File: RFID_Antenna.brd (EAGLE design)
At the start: 25.4 x 43.2 mm, 25 parts, among them J1 U.FL

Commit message: Caopy Murata Design w/ Transparency for x02
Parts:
- C1, C2, C3, C4, C5, C6, L1, R1: device special_parts:0402 -> special_parts:0402_MURATA
- L2, L3, L4, L5: device special_parts:0603 -> special_parts:0603_MURATA
- moved L5 4.23 mm to (11.9, 18.1)
- moved C6 4.19 mm to (14.4, 18.1)
- moved C5 4.14 mm to (11.6, 19.4)
- moved L4 3.97 mm to (14.1, 19.4)
- moved L1 3.65 mm to (13.0, 20.5)
- moved J1 3.50 mm to (12.5, 14.5)
- moved C3 3.34 mm to (12.5, 22.0)
- moved C4 3.31 mm to (13.3, 22.1)
- moved L2 2.91 mm to (11.4, 21.1)
- moved L3 2.81 mm to (14.6, 21.2)
- moved C1 2.61 mm to (12.1, 23.2)
- moved C2 2.52 mm to (13.7, 23.2)
- moved R1 0.46 mm to (13.0, 24.1)
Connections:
- net A1: now also C1.P$1, L2.P$2, R1.P$1; no longer C1.1, L2.2, R1.1
- net A2: now also C2.P$2, L3.P$2, R1.P$2; no longer C2.2, L3.2, R1.2
- net C1C3: now also C1.P$2, C3.P$1; no longer C1.2, C3.1
- net C2C4: now also C2.P$1, C4.P$1; no longer C2.1, C4.1
- net C3C4: now also C3.P$2, C4.P$2; no longer C3.2, C4.2
- net GND: now also C5.P$1, L4.P$2; no longer C5.1, L4.2
- net L5C6: now also C6.P$2, L5.P$1; no longer C6.2, L5.1
- net N$6: now also C6.P$1, L1.P$2, L3.P$1, L4.P$1; no longer C6.1, L1.2, L3.1, L4.1
- net N$7: now also C5.P$2, L1.P$1, L2.P$1, L5.P$2; no longer C5.2, L1.1, L2.1, L5.2
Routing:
- net A1: track 5.55 -> 1.44 mm
- net A2: track 5.61 -> 2.81 mm
- net N$6: track 5.93 -> 3.62 mm
- net N$7: track 5.50 -> 3.61 mm
- net GND: track 1.84 -> 2.58 mm, vias 19 -> 25
- net C2C4: track 1.37 -> 0.75 mm
- net C1C3: track 1.37 -> 0.78 mm
- net C3C4: track 1.40 -> 0.83 mm

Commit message: Add production for x02
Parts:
- moved FRAME1 113.1 mm to (-15.2, -66.0)
- moved U$2 66.1 mm to (-34.3, -5.08)
- moved U$11 12.7 mm to (12.7, 25.4)
- moved C2 5.08 mm to (13.7, 18.1)
- moved C3 5.08 mm to (12.5, 17.0)
- moved L3 5.08 mm to (14.6, 16.1)
- moved U$1 5.08 mm to (12.7, 26.7)
- moved U$3 5.08 mm to (12.7, 28.6)
- moved U$4 5.08 mm to (12.7, 28.6)
- moved U$5 5.08 mm to (6.83, 25.9)
- moved U$6 5.08 mm to (18.5, 25.9)
- moved J1 5.08 mm to (12.5, 9.42)
- moved L1 5.08 mm to (13.0, 15.4)
- moved L4 5.08 mm to (14.1, 14.3)
- moved L5 5.08 mm to (11.9, 13.0)
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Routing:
- net GND: track 2.58 -> 2.80 mm, vias 25 -> 24
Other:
- board size 25.4 x 43.2 mm -> 25.4 x 38.1 mm
- board text added: "Owen Lyke"

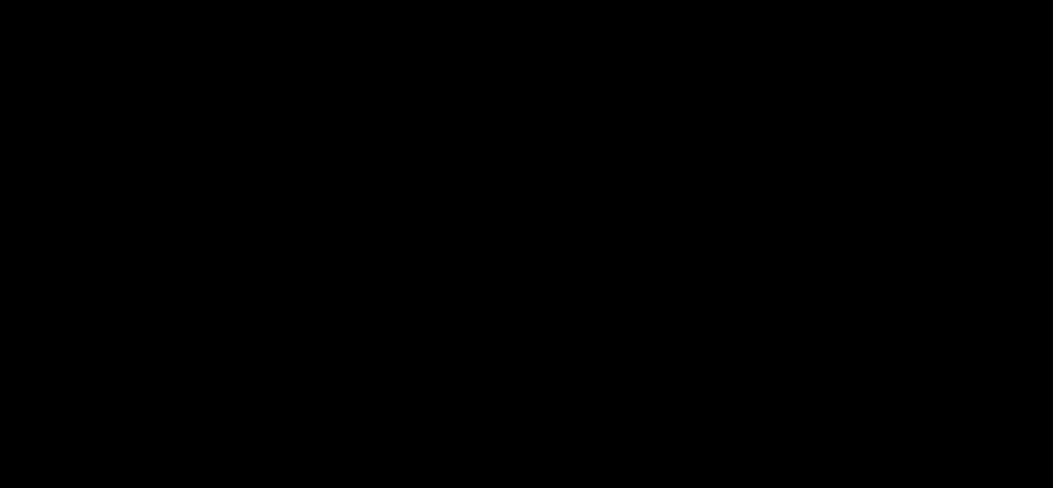
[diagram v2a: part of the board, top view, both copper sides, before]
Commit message: Prettified schematic (and fixed component values)
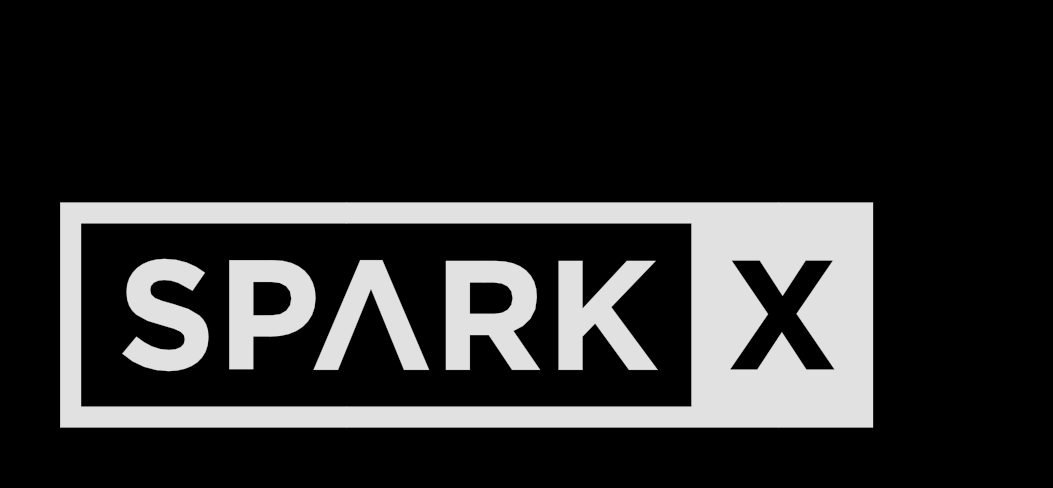
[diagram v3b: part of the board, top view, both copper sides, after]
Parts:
- added U$12: SPARKX-LOGO6, SparkX:SPARKX-XLARGE
- C1, C2: value 9.3 pF -> 5.0 pF
- C3, C4: value 9.0 pF -> 5.0 pF
- C5, C6: value 5.66 pF -> 2.4 pF
- L1: value 0.26 uH -> 19 nH
- L2, L3: value 0.26 uH -> 24 nH
- L4, L5: value 0.24 uH -> 11 nH
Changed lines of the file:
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@@
 <grid distance="0.05" unitdist="inch" unit="inch" style="lines" multiple="1" display="yes" altdistance="0.005" altunitdist="inch" altunit="inch"/>
 <layers>
-<layer number="1" name="Top" color="4" fill="1" visible="no" active="yes"/>
-<layer number="16" name="Bottom" color="1" fill="1" visible="no" active="yes"/>
-<layer number="17" name="Pads" color="2" fill="1" visible="no" active="yes"/>
-<layer number="18" name="Vias" color="2" fill="1" visible="no" active="yes"/>
-<layer number="19" name="Unrouted" color="6" fill="1" visible="no" active="yes"/>
+<layer number="1" name="Top" color="4" fill="1" visible="yes" active="yes"/>
+<layer number="16" name="Bottom" color="1" fill="1" visible="yes" active="yes"/>
+<layer number="17" name="Pads" color="2" fill="1" visible="yes" active="yes"/>
+<layer number="18" name="Vias" color="2" fill="1" visible="yes" active="yes"/>
+<layer number="19" name="Unrouted" color="6" fill="1" visible="yes" active="yes"/>
 <layer number="20" name="Dimension" color="15" fill="1" visible="yes" active="yes"/>
-<layer number="21" name="tPlace" color="16" fill="1" visible="no" active="yes"/>
-<layer number="22" name="bPlace" color="14" fill="1" visible="no" active="yes"/>
-<layer number="23" name="tOrigins" color="15" fill="1" visible="no" active="yes"/>
-<layer number="24" name="bOrigins" color="15" fill="1" visible="no" active="yes"/>
+<layer number="21" name="tPlace" color="16" fill="1" visible="yes" active="yes"/>
+<layer number="22" name="bPlace" color="14" fill="1" visible="yes" active="yes"/>
+<layer number="23" name="tOrigins" color="15" fill="1" visible="yes" active="yes"/>
+<layer number="24" name="bOrigins" color="15" fill="1" visible="yes" active="yes"/>
 <layer number="25" name="tNames" color="7" fill="1" visible="no" active="yes"/>
 <layer number="26" name="bNames" color="7" fill="1" visible="no" active="yes"/>
 <layer number="27" name="tValues" color="7" fill="1" visible="no" active="yes"/>
 <layer number="28" name="bValues" color="7" fill="1" visible="no" active="yes"/>
-<layer number="29" name="tStop" color="7" fill="3" visible="yes" active="yes"/>
+<layer number="29" name="tStop" color="7" fill="3" visible="no" active="yes"/>
 <layer number="30" name="bStop" color="7" fill="6" visible="no" active="yes"/>
 <layer number="31" name="tCream" color="7" fill="4" visible="no" active="yes"/>
@@
 <layer number="43" name="vRestrict" color="2" fill="10" visible="no" active="yes"/>
 <layer number="44" name="Drills" color="7" fill="1" visible="no" active="yes"/>
-<layer number="45" name="Holes" color="7" fill="1" visible="no" active="yes"/>
+<layer number="45" name="Holes" color="7" fill="1" visible="yes" active="yes"/>
 <layer number="46" name="Milling" color="3" fill="1" visible="no" active="yes"/>
-<layer number="47" name="Measures" color="7" fill="1" visible="no" active="yes"/>
+<layer number="47" name="Measures" color="7" fill="1" visible="yes" active="yes"/>
 <layer number="48" name="Document" color="7" fill="1" visible="no" active="yes"/>
 <layer number="49" name="Reference" color="7" fill="1" visible="no" active="yes"/>
 <layer number="50" name="dxf" color="7" fill="1" visible="no" active="yes"/>
-<layer number="51" name="tDocu" color="6" fill="1" visible="no" active="yes"/>
+<layer number="51" name="tDocu" color="6" fill="1" visible="yes" active="yes"/>
 <layer number="52" name="bDocu" color="7" fill="1" visible="no" active="yes"/>
 <layer number="91" name="Nets" color="2" fill="1" visible="no" active="no"/>
@@
 </autorouter>
 <elements>
-<element name="C1" library="special_parts" package="0402_MURATA" value="9.3 pF" x="12.1462" y="18.1292"/>
-<element name="C2" library="special_parts" package="0402_MURATA" value="9.3 pF" x="13.7462" y="18.1242"/>
-<element name="C3" library="special_parts" package="0402_MURATA" value="9.0 pF" x="12.5192" y="16.9652" rot="R270"/>
-<element name="C4" library="special_parts" package="0402_MURATA" value="9.0 pF" x="13.3412" y="16.9752" rot="R270"/>
-<element name="C5" library="special_parts" package="0402_MURATA" value="5.66 pF" x="11.6212" y="14.3352" rot="R180"/>
-<element name="C6" library="special_parts" package="0402_MURATA" value="5.66 pF" x="14.3952" y="13.0242" rot="R180"/>
+<element name="C1" library="special_parts" package="0402_MURATA" value="5.0 pF" x="12.1462" y="18.1292"/>
+<element name="C2" library="special_parts" package="0402_MURATA" value="5.0 pF" x="13.7462" y="18.1242"/>
+<element name="C3" library="special_parts" package="0402_MURATA" value="5.0 pF" x="12.5192" y="16.9652" rot="R270"/>
+<element name="C4" library="special_parts" package="0402_MURATA" value="5.0 pF" x="13.3412" y="16.9752" rot="R270"/>
+<element name="C5" library="special_parts" package="0402_MURATA" value="2.4 pF" x="11.6212" y="14.3352" rot="R180"/>
+<element name="C6" library="special_parts" package="0402_MURATA" value="2.4 pF" x="14.3952" y="13.0242" rot="R180"/>
 <element name="FRAME1" library="SparkFun-Aesthetics" package="CREATIVE_COMMONS" value="FRAME-LETTER" x="-15.24" y="-66.04">
 <attribute name="DESIGNER" value="Owen Lyke" x="-15.24" y="-66.04" size="1.778" layer="27" display="off"/>
@@
 <attribute name="SF_ID" value="WRL-09144" x="12.5492" y="9.4182" size="1.778" layer="27" rot="R90" display="off"/>
 </element>
-<element name="L1" library="special_parts" package="0402_MURATA" value="0.26 uH" x="13.0092" y="15.3952"/>
-<element name="L2" library="special_parts" package="0603_MURATA" value="0.26 uH" x="11.45" y="16.07" rot="R90"/>
-<element name="L3" library="special_parts" package="0603_MURATA" value="0.26 uH" x="14.575" y="16.08" rot="R90"/>
-<element name="L4" library="special_parts" package="0603_MURATA" value="0.24 uH" x="14.0862" y="14.3282" rot="R180"/>
-<element name="L5" library="special_parts" package="0603_MURATA" value="0.24 uH" x="11.8592" y="13.0392" rot="R180"/>
+<element name="L1" library="special_parts" package="0402_MURATA" value="19 nH" x="13.0092" y="15.3952"/>
+<element name="L2" library="special_parts" package="0603_MURATA" value="24 nH" x="11.45" y="16.07" rot="R90"/>
+<element name="L3" library="special_parts" package="0603_MURATA" value="24 nH" x="14.575" y="16.08" rot="R90"/>
+<element name="L4" library="special_parts" package="0603_MURATA" value="11 nH" x="14.0862" y="14.3282" rot="R180"/>
+<element name="L5" library="special_parts" package="0603_MURATA" value="11 nH" x="11.8592" y="13.0392" rot="R180"/>
 <element name="R1" library="special_parts" package="0402_MURATA" value="4.28k" x="12.9762" y="19.0422"/>
 <element name="U$1" library="special_parts" package="ANT" value="ANTENNA" x="12.7112" y="26.6632"/>
@@
 <element name="U$10" library="SparkFun-Aesthetics" package="OSHW-LOGO-S" value="" x="12.7" y="21.082"/>
 <element name="U$11" library="SparkX" package="QWIIC_BOARD_MOUNT_HOLES" value="" x="12.7" y="25.4" rot="MR0"/>
+<element name="U$12" library="SparkX" package="SPARKX-XLARGE" value="SPARKX-LOGO6" x="-21.59" y="-71.12"/>
 </elements>
 <signals>

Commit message: Updated parts with PROD_ID and Eagle Library for production
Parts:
- C1, C2, C3, C4, C5, C6: device special_parts:0402_MURATA -> SparkFun-Capacitors:0402_MURATA
- L1: device special_parts:0402_MURATA -> SparkFun-Coils:0402_MURATA
- L2, L3, L4, L5: device special_parts:0603_MURATA -> SparkFun-Coils:0603_MURATA
- R1: value 4.28k -> 4.3k; device special_parts:0402_MURATA -> SparkFun-Resistors:0402_MURATA
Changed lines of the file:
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@@
 <layer number="96" name="Values" color="7" fill="1" visible="no" active="no"/>
 <layer number="2" name="Route2" color="16" fill="1" visible="no" active="no"/>
+<layer number="3" name="Route3" color="4" fill="3" visible="no" active="no"/>
+<layer number="4" name="Route4" color="1" fill="4" visible="no" active="no"/>
+<layer number="5" name="Route5" color="4" fill="4" visible="no" active="no"/>
+<layer number="6" name="Route6" color="1" fill="8" visible="no" active="no"/>
+<layer number="7" name="Route7" color="4" fill="8" visible="no" active="no"/>
+<layer number="8" name="Route8" color="1" fill="2" visible="no" active="no"/>
+<layer number="9" name="Route9" color="4" fill="2" visible="no" active="no"/>
+<layer number="10" name="Route10" color="1" fill="7" visible="no" active="no"/>
+<layer number="11" name="Route11" color="4" fill="7" visible="no" active="no"/>
+<layer number="12" name="Route12" color="1" fill="5" visible="no" active="no"/>
+<layer number="13" name="Route13" color="4" fill="5" visible="no" active="no"/>
+<layer number="14" name="Route14" color="1" fill="6" visible="no" active="no"/>
 <layer number="15" name="Route15" color="23" fill="1" visible="no" active="no"/>
 <layer number="53" name="tGND_GNDA" color="7" fill="9" visible="no" active="no"/>
@@
 </autorouter>
 <elements>
-<element name="C1" library="special_parts" package="0402_MURATA" value="5.0 pF" x="12.1462" y="18.1292" smashed="yes"/>
-<element name="C2" library="special_parts" package="0402_MURATA" value="5.0 pF" x="13.7462" y="18.1242" smashed="yes"/>
-<element name="C3" library="special_parts" package="0402_MURATA" value="5.0 pF" x="12.5192" y="16.9652" smashed="yes" rot="R270"/>
-<element name="C4" library="special_parts" package="0402_MURATA" value="5.0 pF" x="13.3412" y="16.9752" smashed="yes" rot="R270"/>
-<element name="C5" library="special_parts" package="0402_MURATA" value="2.4 pF" x="11.6212" y="14.3352" smashed="yes" rot="R180"/>
-<element name="C6" library="special_parts" package="0402_MURATA" value="2.4 pF" x="14.3952" y="13.0242" smashed="yes" rot="R180"/>
+<element name="C1" library="SparkFun-Capacitors" package="0402_MURATA" value="5.0 pF" x="12.1462" y="18.1292" smashed="yes">
+<attribute name="PROD_ID" value="CAP-14350" x="12.1462" y="18.1292" size="1.778" layer="27" display="off"/>
+<attribute name="VALUE" value="5.0 pF" x="12.1462" y="18.1292" size="1.778" layer="27" display="off"/>
+</element>
+<element name="C2" library="SparkFun-Capacitors" package="0402_MURATA" value="5.0 pF" x="13.7462" y="18.1242" smashed="yes">
+<attribute name="PROD_ID" value="CAP-14350" x="13.7462" y="18.1242" size="1.778" layer="27" display="off"/>
+<attribute name="VALUE" value="5.0 pF" x="13.7462" y="18.1242" size="1.778" layer="27" display="off"/>
+</element>
+<element name="C3" library="SparkFun-Capacitors" package="0402_MURATA" value="5.0 pF" x="12.5192" y="16.9652" smashed="yes" rot="R270">
+<attribute name="PROD_ID" value="CAP-14350" x="12.5192" y="16.9652" size="1.778" layer="27" rot="R270" display="off"/>
+<attribute name="VALUE" value="5.0 pF" x="12.5192" y="16.9652" size="1.778" layer="27" rot="R270" display="off"/>
+</element>
+<element name="C4" library="SparkFun-Capacitors" package="0402_MURATA" value="5.0 pF" x="13.3412" y="16.9752" smashed="yes" rot="R270">
+<attribute name="PROD_ID" value="CAP-14350" x="13.3412" y="16.9752" size="1.778" layer="27" rot="R270" display="off"/>
+<attribute name="VALUE" value="5.0 pF" x="13.3412" y="16.9752" size="1.778" layer="27" rot="R270" display="off"/>
+</element>
+<element name="C5" library="SparkFun-Capacitors" package="0402_MURATA" value="2.4 pF" x="11.6212" y="14.3352" smashed="yes" rot="R180">
+<attribute name="PROD_ID" value="CAP-14351" x="11.6212" y="14.3352" size="1.778" layer="27" rot="R180" display="off"/>
+<attribute name="VALUE" value="2.4 pF" x="11.6212" y="14.3352" size="1.778" layer="27" rot="R180" display="off"/>
+</element>
+<element name="C6" library="SparkFun-Capacitors" package="0402_MURATA" value="2.4 pF" x="14.3952" y="13.0242" smashed="yes" rot="R180">
+<attribute name="PROD_ID" value="CAP-14351" x="14.3952" y="13.0242" size="1.778" layer="27" rot="R180" display="off"/>
+<attribute name="VALUE" value="2.4 pF" x="14.3952" y="13.0242" size="1.778" layer="27" rot="R180" display="off"/>
+</element>
 <element name="FRAME1" library="SparkFun-Aesthetics" package="CREATIVE_COMMONS" value="FRAME-LETTER" x="-15.24" y="-66.04" smashed="yes">
 <attribute name="DESIGNER" value="Owen Lyke" x="-15.24" y="-66.04" size="1.778" layer="27" display="off"/>
@@
 <attribute name="VALUE" x="15.0892" y="8.1482" size="0.6096" layer="27" font="vector" ratio="20" rot="R90" align="top-left"/>
 </element>
-<element name="L1" library="special_parts" package="0402_MURATA" value="19 nH" x="13.0092" y="15.3952" smashed="yes"/>
-<element name="L2" library="special_parts" package="0603_MURATA" value="24 nH" x="11.45" y="16.07" smashed="yes" rot="R90"/>
-<element name="L3" library="special_parts" package="0603_MURATA" value="24 nH" x="14.575" y="16.08" smashed="yes" rot="R90"/>
-<element name="L4" library="special_parts" package="0603_MURATA" value="11 nH" x="14.0862" y="14.3282" smashed="yes" rot="R180"/>
-<element name="L5" library="special_parts" package="0603_MURATA" value="11 nH" x="11.8592" y="13.0392" smashed="yes" rot="R180"/>
-<element name="R1" library="special_parts" package="0402_MURATA" value="4.28k" x="12.9762" y="19.0422" smashed="yes"/>
+<element name="L1" library="SparkFun-Coils" package="0402_MURATA" value="19 nH" x="13.0092" y="15.3952" smashed="yes">
+<attribute name="PROD_ID" value="NDUC-14352" x="13.0092" y="15.3952" size="1.778" layer="27" display="off"/>
+<attribute name="VALUE" value="19 nH" x="13.0092" y="15.3952" size="1.778" layer="27" display="off"/>
+</element>
+<element name="L2" library="SparkFun-Coils" package="0603_MURATA" value="24 nH" x="11.45" y="16.07" smashed="yes" rot="R90">
+<attribute name="PROD_ID" value="NDUC-14353" x="11.45" y="16.07" size="1.778" layer="27" rot="R90" display="off"/>
+<attribute name="VALUE" value="24 nH" x="11.45" y="16.07" size="1.778" layer="27" rot="R90" display="off"/>
+</element>
+<element name="L3" library="SparkFun-Coils" package="0603_MURATA" value="24 nH" x="14.575" y="16.08" smashed="yes" rot="R90">
+<attribute name="PROD_ID" value="NDUC-14353" x="14.575" y="16.08" size="1.778" layer="27" rot="R90" display="off"/>
+<attribute name="VALUE" value="24 nH" x="14.575" y="16.08" size="1.778" layer="27" rot="R90" display="off"/>
+</element>
+<element name="L4" library="SparkFun-Coils" package="0603_MURATA" value="11 nH" x="14.0862" y="14.3282" smashed="yes" rot="R180">
+<attribute name="PROD_ID" value="NDUC-14354" x="14.0862" y="14.3282" size="1.778" layer="27" rot="R180" display="off"/>
+<attribute name="VALUE" value="11 nH" x="14.0862" y="14.3282" size="1.778" layer="27" rot="R180" display="off"/>
+</element>
+<element name="L5" library="SparkFun-Coils" package="0603_MURATA" value="11 nH" x="11.8592" y="13.0392" smashed="yes" rot="R180">
+<attribute name="PROD_ID" value="NDUC-14354" x="11.8592" y="13.0392" size="1.778" layer="27" rot="R180" display="off"/>
+<attribute name="VALUE" value="11 nH" x="11.8592" y="13.0392" size="1.778" layer="27" rot="R180" display="off"/>
+</element>
+<element name="R1" library="SparkFun-Resistors" package="0402_MURATA" value="4.3k" x="12.9762" y="19.0422" smashed="yes">
+<attribute name="PROD_ID" value="RES-14355" x="12.9762" y="19.0422" size="1.778" layer="27" display="off"/>
+<attribute name="VALUE" value="4.3k" x="12.9762" y="19.0422" size="1.778" layer="27" display="off"/>
+</element>
 <element name="U$1" library="special_parts" package="ANT" value="ANTENNA" x="12.7112" y="26.6632" smashed="yes"/>
 <element name="U$2" library="SparkFun-Aesthetics" package="ORDERING_INSTRUCTIONS" value="SPECIAL_INSTRUCTIONS-ORDERING" x="-34.29" y="-5.08" smashed="yes"/>
